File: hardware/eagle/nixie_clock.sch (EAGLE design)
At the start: 61 parts, among them IC1 74141N, IC10 7477N, IC11 74141N, IC12 7477N, IC13 74AC11238, IC2 7477N, IC3 74141N, IC4 7477N, IC5 74141N, IC6 7477N, IC7 74141N, IC8 7477N, IC9 74141N, J1_180V 22-27-2021-02, J1_5V1 22-27-2021-02, J1_5V2 22-27-2021-02

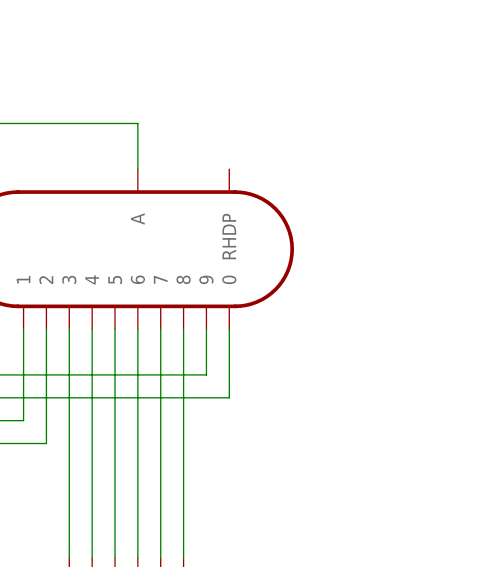
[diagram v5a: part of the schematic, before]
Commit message: FreeCad nixie model
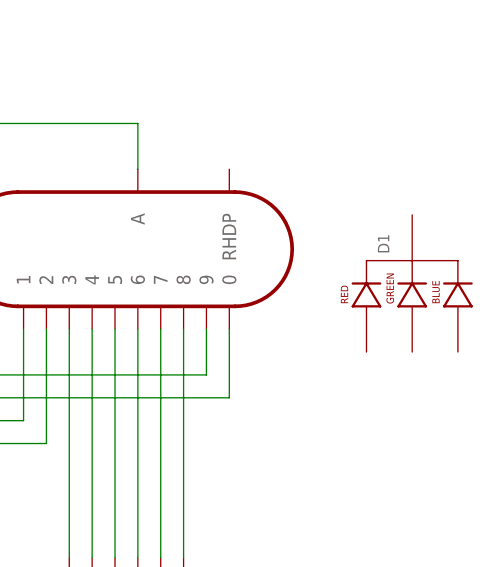
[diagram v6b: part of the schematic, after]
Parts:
- added D1: LED-RGB-CC-THRUCLEAR, SparkFun-LED:LED-RGB-CC-THRUCLEAR
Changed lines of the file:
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@@
 <layer number="48" name="Document" color="7" fill="1" visible="no" active="no"/>
 <layer number="49" name="Reference" color="7" fill="1" visible="no" active="no"/>
+<layer number="50" name="dxf" color="7" fill="1" visible="no" active="no"/>
 <layer number="51" name="tDocu" color="7" fill="1" visible="no" active="no"/>
 <layer number="52" name="bDocu" color="7" fill="1" visible="no" active="no"/>
+<layer number="53" name="tGND_GNDA" color="7" fill="9" visible="no" active="no"/>
+<layer number="54" name="bGND_GNDA" color="1" fill="9" visible="no" active="no"/>
+<layer number="56" name="wert" color="7" fill="1" visible="no" active="no"/>
+<layer number="57" name="tCAD" color="7" fill="1" visible="no" active="no"/>
+<layer number="59" name="tCarbon" color="7" fill="1" visible="no" active="no"/>
+<layer number="60" name="bCarbon" color="7" fill="1" visible="no" active="no"/>
+<layer number="90" name="Modules" color="5" fill="1" visible="no" active="no"/>
 <layer number="91" name="Nets" color="2" fill="1" visible="yes" active="yes"/>
 <layer number="92" name="Busses" color="1" fill="1" visible="yes" active="yes"/>
@@
 <layer number="98" name="Guide" color="6" fill="1" visible="yes" active="yes"/>
 <layer number="99" name="SpiceOrder" color="5" fill="1" visible="yes" active="yes"/>
+<layer number="100" name="Muster" color="7" fill="1" visible="no" active="no"/>
+<layer number="101" name="Patch_Top" color="12" fill="4" visible="yes" active="yes"/>
+<layer number="102" name="Vscore" color="7" fill="1" visible="yes" active="yes"/>
+<layer number="103" name="tMap" color="7" fill="1" visible="yes" active="yes"/>
+<layer number="104" name="Name" color="16" fill="1" visible="yes" active="yes"/>
+<layer number="105" name="tPlate" color="7" fill="1" visible="yes" active="yes"/>
+<layer number="106" name="bPlate" color="7" fill="1" visible="yes" active="yes"/>
+<layer number="107" name="Crop" color="7" fill="1" visible="yes" active="yes"/>
+<layer number="108" name="tplace-old" color="10" fill="1" visible="yes" active="yes"/>
+<layer number="109" name="ref-old" color="11" fill="1" visible="yes" active="yes"/>
+<layer number="110" name="fp0" color="7" fill="1" visible="yes" active="yes"/>
+<layer number="111" name="LPC17xx" color="7" fill="1" visible="yes" active="yes"/>
+<layer number="112" name="tSilk" color="7" fill="1" visible="yes" active="yes"/>
+<layer number="113" name="IDFDebug" color="4" fill="1" visible="yes" active="yes"/>
+<layer number="116" name="Patch_BOT" color="9" fill="4" visible="yes" active="yes"/>
+<layer number="118" name="Rect_Pads" color="7" fill="1" visible="yes" active="yes"/>
+<layer number="121" name="_tsilk" color="7" fill="1" visible="yes" active="yes"/>
+<layer number="122" name="_bsilk" color="7" fill="1" visible="yes" active="yes"/>
+<layer number="123" name="tTestmark" color="7" fill="1" visible="yes" active="yes"/>
+<layer number="124" name="bTestmark" color="7" fill="1" visible="yes" active="yes"/>
+<layer number="125" name="_tNames" color="7" fill="1" visible="yes" active="yes"/>
+<layer number="126" name="_bNames" color="7" fill="1" visible="yes" active="yes"/>
+<layer number="127" name="_tValues" color="7" fill="1" visible="yes" active="yes"/>
+<layer number="128" name="_bValues" color="7" fill="1" visible="yes" active="yes"/>
+<layer number="129" name="Mask" color="7" fill="1" visible="yes" active="yes"/>
+<layer number="131" name="tAdjust" color="7" fill="1" visible="yes" active="yes"/>
+<layer number="132" name="bAdjust" color="7" fill="1" visible="yes" active="yes"/>
+<layer number="144" name="Drill_legend" color="7" fill="1" visible="yes" active="yes"/>
+<layer number="150" name="Notes" color="7" fill="1" visible="yes" active="yes"/>
+<layer number="151" name="HeatSink" color="7" fill="1" visible="yes" active="yes"/>
+<layer number="152" name="_bDocu" color="7" fill="1" visible="yes" active="yes"/>
+<layer number="153" name="FabDoc1" color="7" fill="1" visible="yes" active="yes"/>
+<layer number="154" name="FabDoc2" color="7" fill="1" visible="yes" active="yes"/>
+<layer number="155" name="FabDoc3" color="7" fill="1" visible="yes" active="yes"/>
+<layer number="199" name="Contour" color="7" fill="1" visible="yes" active="yes"/>
+<layer number="200" name="200bmp" color="1" fill="10" visible="yes" active="yes"/>
+<layer number="201" name="201bmp" color="2" fill="10" visible="yes" active="yes"/>
+<layer number="202" name="202bmp" color="3" fill="10" visible="yes" active="yes"/>
+<layer number="203" name="203bmp" color="4" fill="10" visible="yes" active="yes"/>
+<layer number="204" name="204bmp" color="5" fill="10" visible="yes" active="yes"/>
+<layer number="205" name="205bmp" color="6" fill="10" visible="yes" active="yes"/>
+<layer number="206" name="206bmp" color="7" fill="10" visible="yes" active="yes"/>
+<layer number="207" name="207bmp" color="8" fill="10" visible="yes" active="yes"/>
+<layer number="208" name="208bmp" color="9" fill="10" visible="yes" active="yes"/>
+<layer number="209" name="209bmp" color="7" fill="1" visible="yes" active="yes"/>
+<layer number="210" name="210bmp" color="7" fill="1" visible="yes" active="yes"/>
+<layer number="211" name="211bmp" color="7" fill="1" visible="yes" active="yes"/>
+<layer number="212" name="212bmp" color="7" fill="1" visible="yes" active="yes"/>
+<layer number="213" name="213bmp" color="7" fill="1" visible="yes" active="yes"/>
+<layer number="214" name="214bmp" color="7" fill="1" visible="yes" active="yes"/>
+<layer number="215" name="215bmp" color="7" fill="1" visible="yes" active="yes"/>
+<layer number="216" name="216bmp" color="7" fill="1" visible="yes" active="yes"/>
+<layer number="217" name="217bmp" color="18" fill="1" visible="no" active="no"/>
+<layer number="218" name="218bmp" color="19" fill="1" visible="no" active="no"/>
+<layer number="219" name="219bmp" color="20" fill="1" visible="no" active="no"/>
+<layer number="220" name="220bmp" color="21" fill="1" visible="no" active="no"/>
+<layer number="221" name="221bmp" color="22" fill="1" visible="no" active="no"/>
+<layer number="222" name="222bmp" color="23" fill="1" visible="no" active="no"/>
+<layer number="223" name="223bmp" color="24" fill="1" visible="no" active="no"/>
+<layer number="224" name="224bmp" color="25" fill="1" visible="no" active="no"/>
+<layer number="225" name="225bmp" color="7" fill="1" visible="yes" active="yes"/>
+<layer number="226" name="226bmp" color="7" fill="1" visible="yes" active="yes"/>
+<layer number="227" name="227bmp" color="7" fill="1" visible="yes" active="yes"/>
+<layer number="228" name="228bmp" color="7" fill="1" visible="yes" active="yes"/>
+<layer number="229" name="229bmp" color="7" fill="1" visible="yes" active="yes"/>
+<layer number="230" name="230bmp" color="7" fill="1" visible="yes" active="yes"/>
+<layer number="231" name="231bmp" color="7" fill="1" visible="yes" active="yes"/>
+<layer number="248" name="Housing" color="7" fill="1" visible="yes" active="yes"/>
+<layer number="249" name="Edge" color="7" fill="1" visible="yes" active="yes"/>
+<layer number="250" name="Descript" color="3" fill="1" visible="no" active="no"/>
+<layer number="251" name="SMDround" color="12" fill="11" visible="no" active="no"/>
+<layer number="254" name="cooling" color="7" fill="1" visible="yes" active="yes"/>
+<layer number="255" name="routoute" color="7" fill="1" visible="yes" active="yes"/>
 </layers>
 <schematic xreflabel="%F%N/%S.%C%R" xrefpart="/%S.%C%R">
@@
 <part name="C15" library="rcl" deviceset="CPOL-EU" device="E3.5-10"/>
 <part name="J1_5V2" library="con-molex" deviceset="22-?-02" device="27-2021"/>
+<part name="D1" library="SparkFun-LED" deviceset="LED-RGB-CC-THRU" device="CLEAR"/>
 </parts>
 <sheets>
@@
 <instance part="J1_5V2" gate="-1" x="213.36" y="25.4" rot="R270"/>
 <instance part="J1_5V2" gate="-2" x="213.36" y="45.72" rot="R90"/>
+<instance part="D1" gate="G$1" x="561.34" y="281.94" rot="R90"/>
 </instances>
 <busses>
